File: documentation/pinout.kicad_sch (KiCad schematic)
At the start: 1 part, among them J1 Conn_02x20_Odd_Even

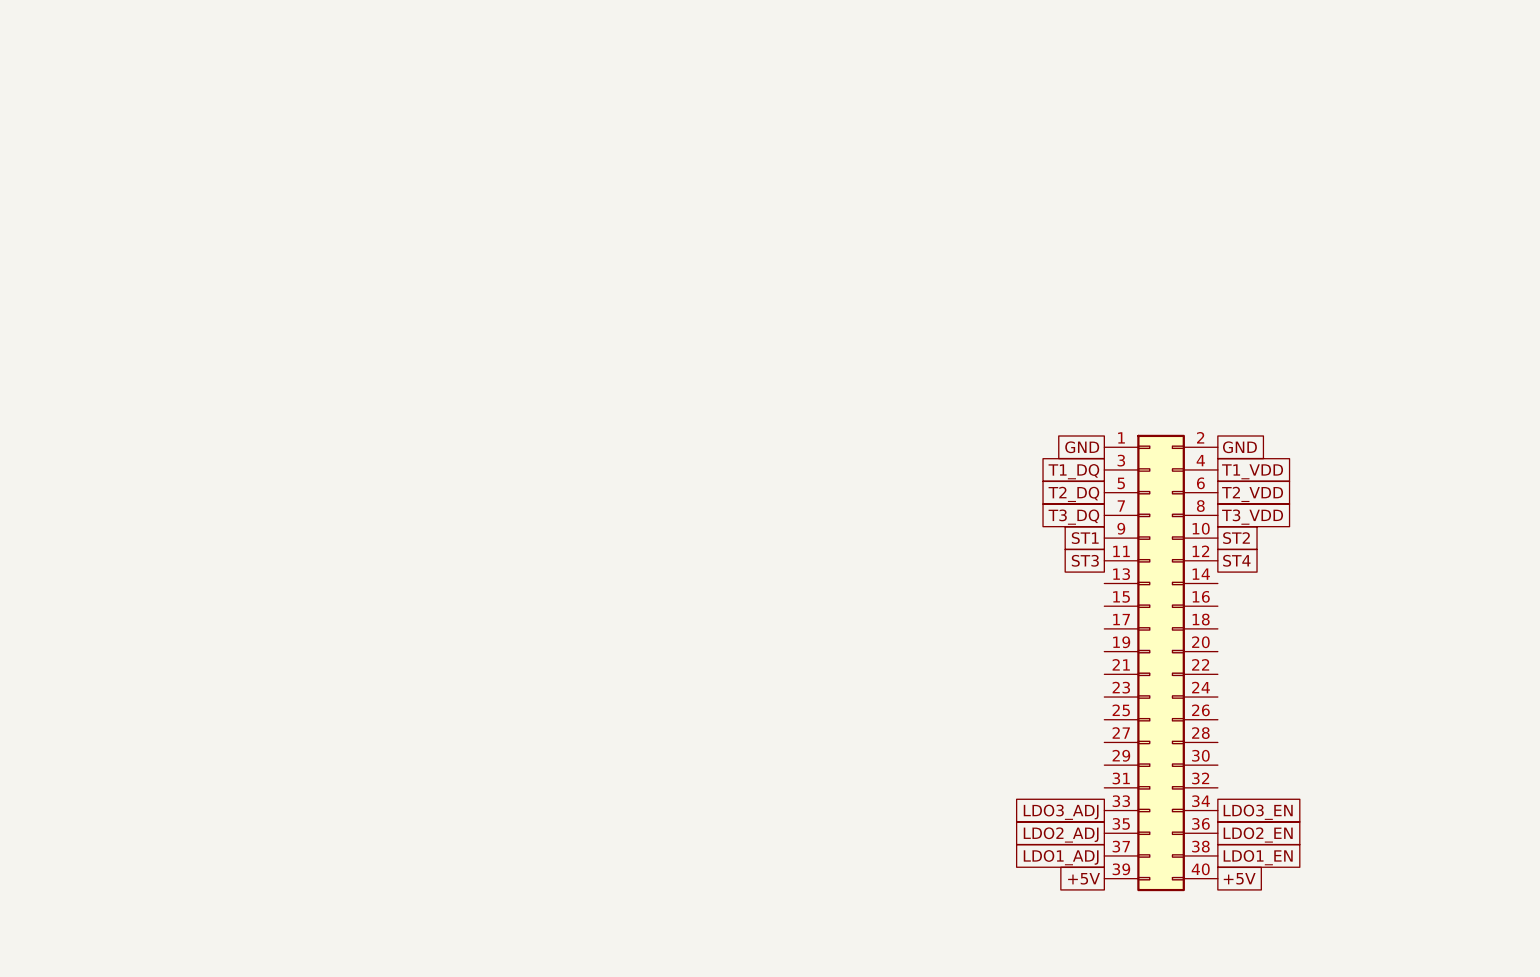
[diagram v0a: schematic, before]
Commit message: Update pinout.kicad_sch
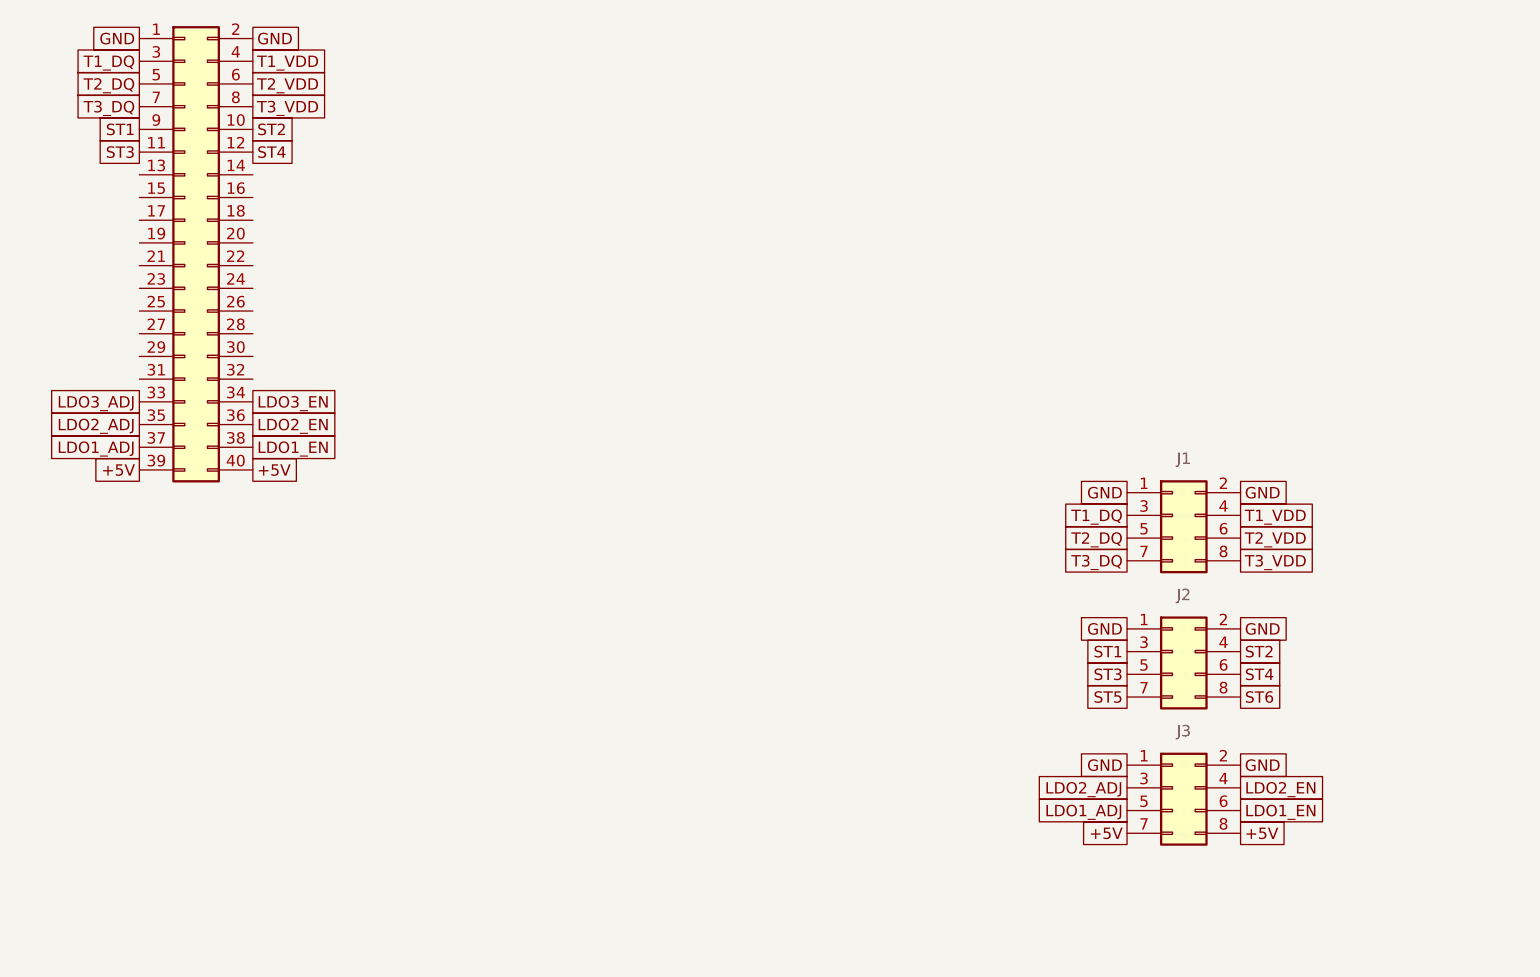
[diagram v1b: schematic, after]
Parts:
- added J1, J2, J3: Conn_02x04_Odd_Even, symbol Connector_Generic:Conn_02x04_Odd_Even
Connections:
- net +5V: now also J3.7 (Pin_7), J3.8 (Pin_8)
- net GND: now also J1.1 (Pin_1), J1.2 (Pin_2), J2.1 (Pin_1), J2.2 (Pin_2), J3.1 (Pin_1), J3.2 (Pin_2)
- net LDO1_ADJ: now also J3.5 (Pin_5)
- net LDO1_EN: now also J3.6 (Pin_6)
- net LDO2_ADJ: now also J3.3 (Pin_3)
- net LDO2_EN: now also J3.4 (Pin_4)
- net ST1: now also J2.3 (Pin_3)
- net ST2: now also J2.4 (Pin_4)
- net ST3: now also J2.5 (Pin_5)
- net ST4: now also J2.6 (Pin_6)
- net T1_DQ: now also J1.3 (Pin_3)
- net T1_VDD: now also J1.4 (Pin_4)
- net T2_DQ: now also J1.5 (Pin_5)
- net T2_VDD: now also J1.6 (Pin_6)
- net T3_DQ: now also J1.7 (Pin_7)
- net T3_VDD: now also J1.8 (Pin_8)
- new net ST5: J2.7 (Pin_7)
- new net ST6: J2.8 (Pin_8)

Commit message: Update pinout.kicad_sch
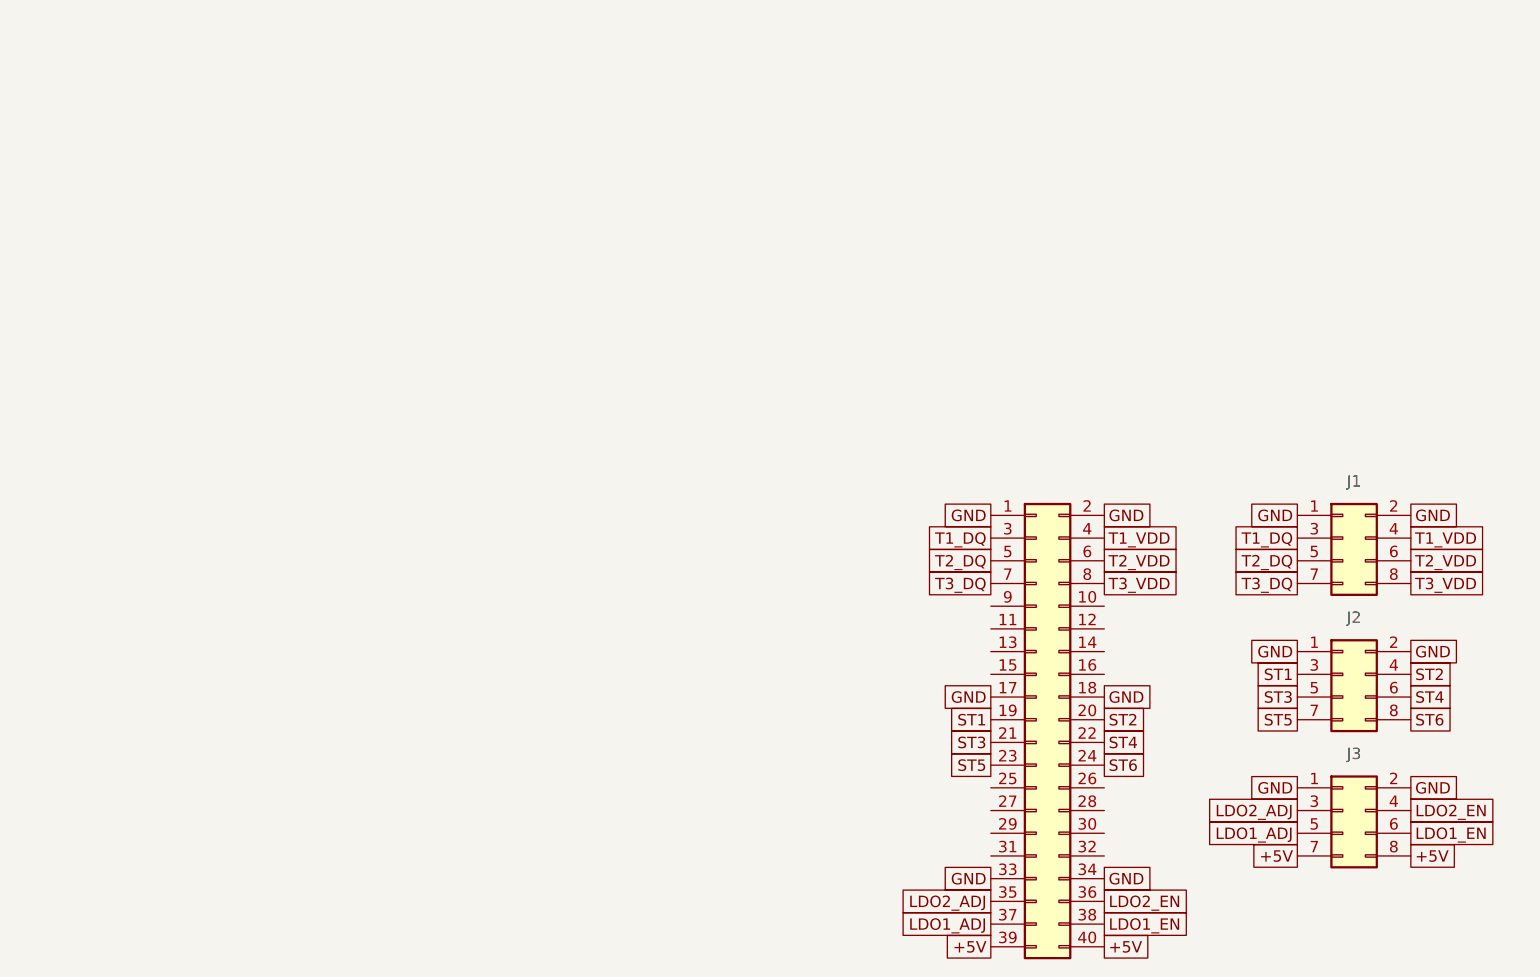
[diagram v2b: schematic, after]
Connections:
- net LDO3_ADJ is gone; now on net GND: J1.33 (Pin_33)
- net LDO3_EN is gone; now on net GND: J1.34 (Pin_34)
- net GND: now also J1.17 (Pin_17), J1.18 (Pin_18)
- net ST1: now also J1.19 (Pin_19); no longer J1.9 (Pin_9)
- net ST2: now also J1.20 (Pin_20); no longer J1.10 (Pin_10)
- net ST3: now also J1.21 (Pin_21); no longer J1.11 (Pin_11)
- net ST4: now also J1.22 (Pin_22); no longer J1.12 (Pin_12)
- net ST5: now also J1.23 (Pin_23)
- net ST6: now also J1.24 (Pin_24)
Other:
- moved on the sheet: J1, J2, J3

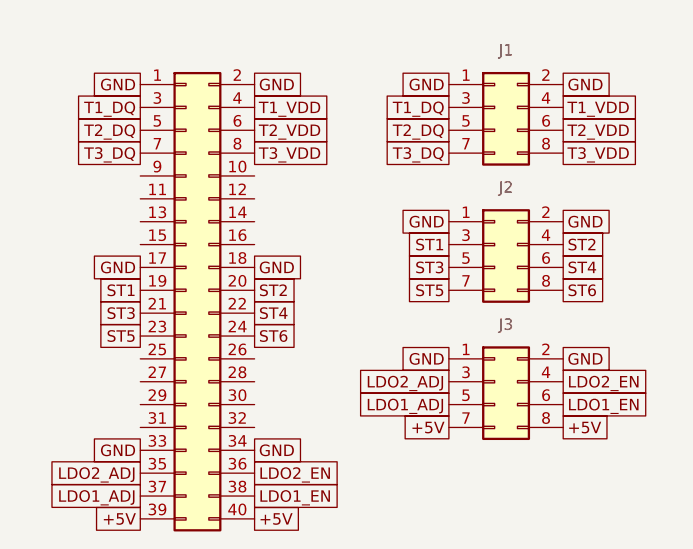
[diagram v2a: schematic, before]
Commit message: Update pinout.kicad_sch
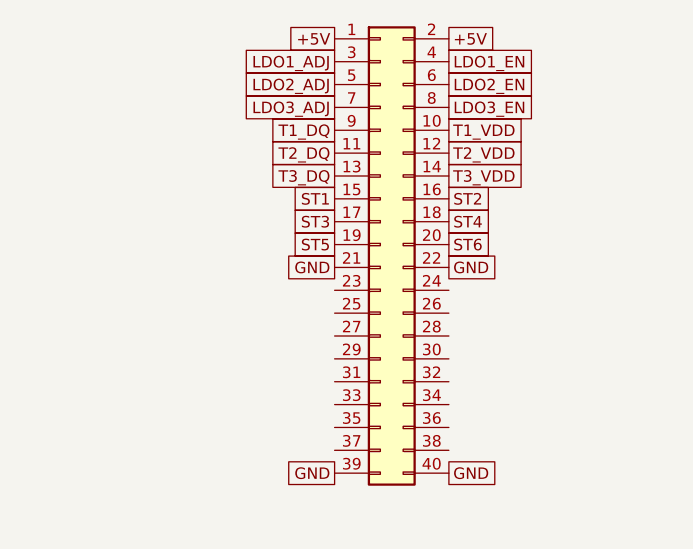
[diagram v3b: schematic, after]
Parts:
- removed J1: Conn_02x20_Odd_Even, Connector_PinHeader_2.54mm:PinHeader_2x20_P2.54mm_Horizontal, symbol Connector_Generic:Conn_02x20_Odd_Even
- removed J1, J2, J3: Conn_02x04_Odd_Even, symbol Connector_Generic:Conn_02x04_Odd_Even
- added J4: Conn_02x20_Odd_Even, symbol Connector_Generic:Conn_02x20_Odd_Even
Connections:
- net +5V: now also J4.1 (Pin_1), J4.2 (Pin_2)
- net GND: now also J4.21 (Pin_21), J4.22 (Pin_22), J4.39 (Pin_39), J4.40 (Pin_40)
- net LDO1_ADJ: now also J4.3 (Pin_3)
- net LDO1_EN: now also J4.4 (Pin_4)
- net LDO2_ADJ: now also J4.5 (Pin_5)
- net LDO2_EN: now also J4.6 (Pin_6)
- net ST1: now also J4.15 (Pin_15)
- net ST2: now also J4.16 (Pin_16)
- net ST3: now also J4.17 (Pin_17)
- net ST4: now also J4.18 (Pin_18)
- net ST5: now also J4.19 (Pin_19)
- net ST6: now also J4.20 (Pin_20)
- net T1_DQ: now also J4.9 (Pin_9)
- net T1_VDD: now also J4.10 (Pin_10)
- net T2_DQ: now also J4.11 (Pin_11)
- net T2_VDD: now also J4.12 (Pin_12)
- net T3_DQ: now also J4.13 (Pin_13)
- net T3_VDD: now also J4.14 (Pin_14)
- new net LDO3_ADJ: J4.7 (Pin_7)
- new net LDO3_EN: J4.8 (Pin_8)

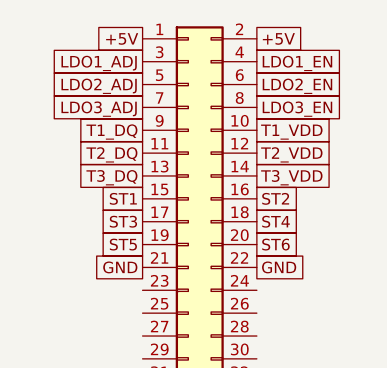
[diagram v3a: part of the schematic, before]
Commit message: Update pinout.kicad_sch
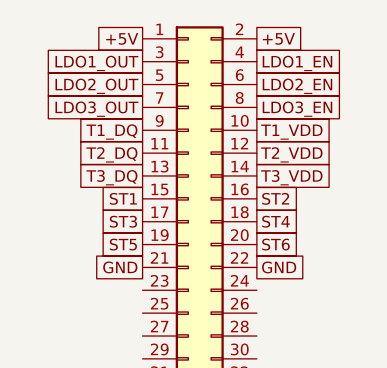
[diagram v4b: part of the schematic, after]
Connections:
- net LDO1_ADJ renamed LDO1_OUT
- net LDO2_ADJ renamed LDO2_OUT
- net LDO3_ADJ renamed LDO3_OUT
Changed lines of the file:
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@@
 		)
 	)
-	(global_label "LDO3_ADJ"
+	(global_label "LDO3_OUT"
 		(shape passive)
 		(at 146.05 78.74 180)
@@
 		)
 		(property "Intersheetrefs" "${INTERSHEET_REFS}"
-			(at 135.8909 78.74 0)
+			(at 134.7418 78.74 0)
 			(effects
 				(font
@@
 		)
 	)
-	(global_label "LDO1_ADJ"
+	(global_label "LDO1_OUT"
 		(shape passive)
 		(at 146.05 73.66 180)
@@
 		)
 		(property "Intersheetrefs" "${INTERSHEET_REFS}"
-			(at 135.0442 73.66 0)
+			(at 134.7418 73.66 0)
 			(effects
 				(font
@@
 		)
 	)
-	(global_label "LDO2_ADJ"
+	(global_label "LDO2_OUT"
 		(shape passive)
 		(at 146.05 76.2 180)
@@
 		)
 		(property "Intersheetrefs" "${INTERSHEET_REFS}"
-			(at 135.8909 76.2 0)
-			(effects
-				(font
+			(at 134.7418 76.2 0)
+			(effects
+				(font

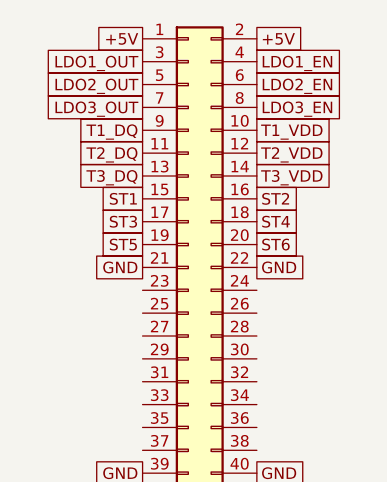
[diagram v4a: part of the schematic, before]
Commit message: Update pinout.kicad_sch
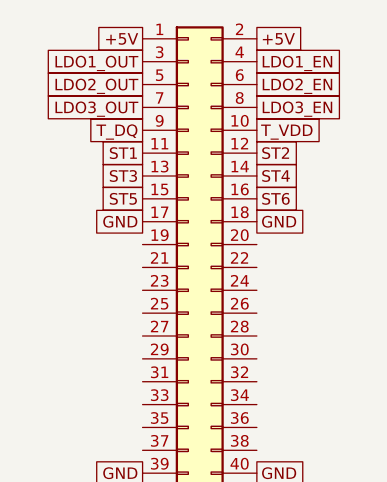
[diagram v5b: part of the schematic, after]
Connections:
- net T2_DQ is gone; now on net ST1: J4.11 (Pin_11)
- net T2_VDD is gone; now on net ST2: J4.12 (Pin_12)
- net T3_DQ is gone; now on net ST3: J4.13 (Pin_13)
- net T3_VDD is gone; now on net ST4: J4.14 (Pin_14)
- net GND: now also J4.17 (Pin_17), J4.18 (Pin_18); no longer J4.21 (Pin_21), J4.22 (Pin_22)
- net ST1: no longer J4.15 (Pin_15)
- net ST2: no longer J4.16 (Pin_16)
- net ST3: no longer J4.17 (Pin_17)
- net ST4: no longer J4.18 (Pin_18)
- net ST5: now also J4.15 (Pin_15); no longer J4.19 (Pin_19)
- net ST6: now also J4.16 (Pin_16); no longer J4.20 (Pin_20)
- net T1_DQ renamed T_DQ
- net T1_VDD renamed T_VDD
